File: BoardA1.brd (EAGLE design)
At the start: 44 x 100.5 mm, 17 parts, among them J1 LOAD_CELL1X03-PTH, J2 FEMALE 2x3, J3 LOAD_CELL1X03-PTH, J5 LOAD_CELL1X03-PTH, J6 LOAD_CELL1X03-PTH

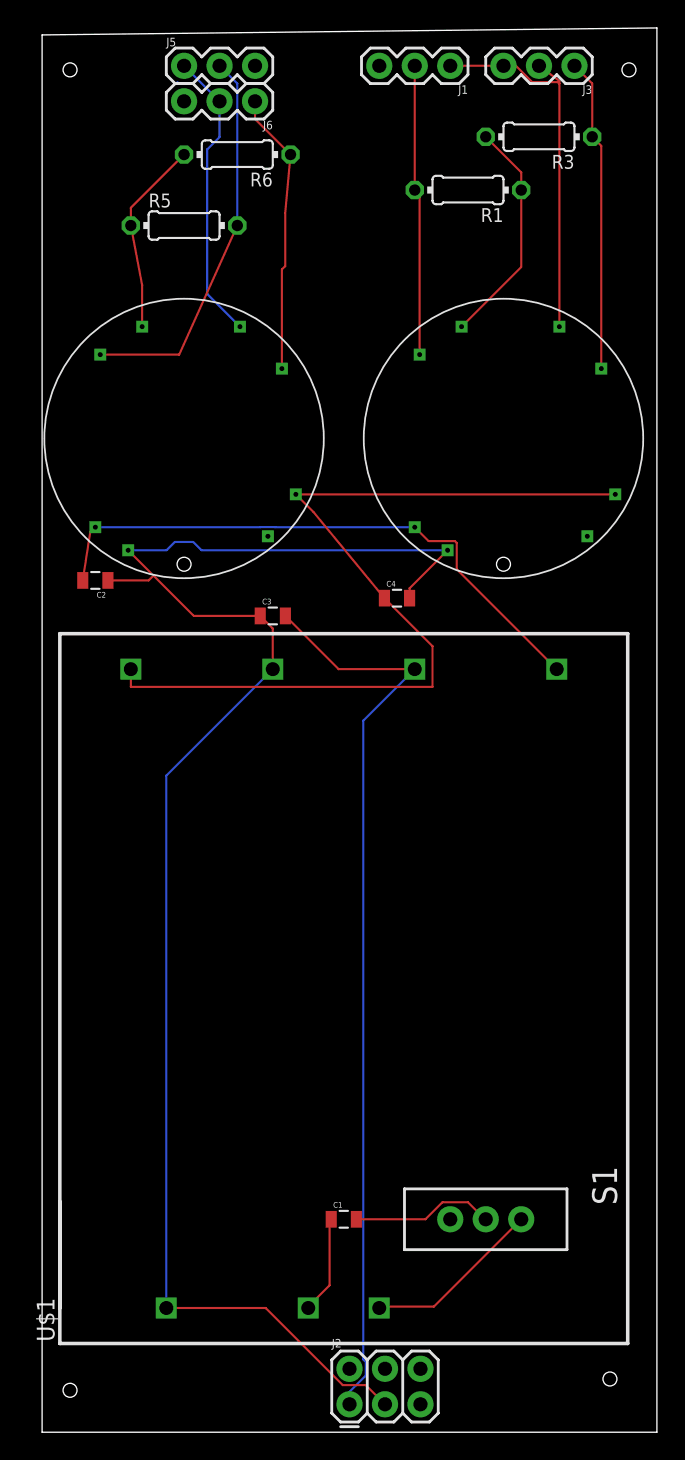
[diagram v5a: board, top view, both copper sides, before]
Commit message: Updated
Fixed Hole placment,connectors, routing issues
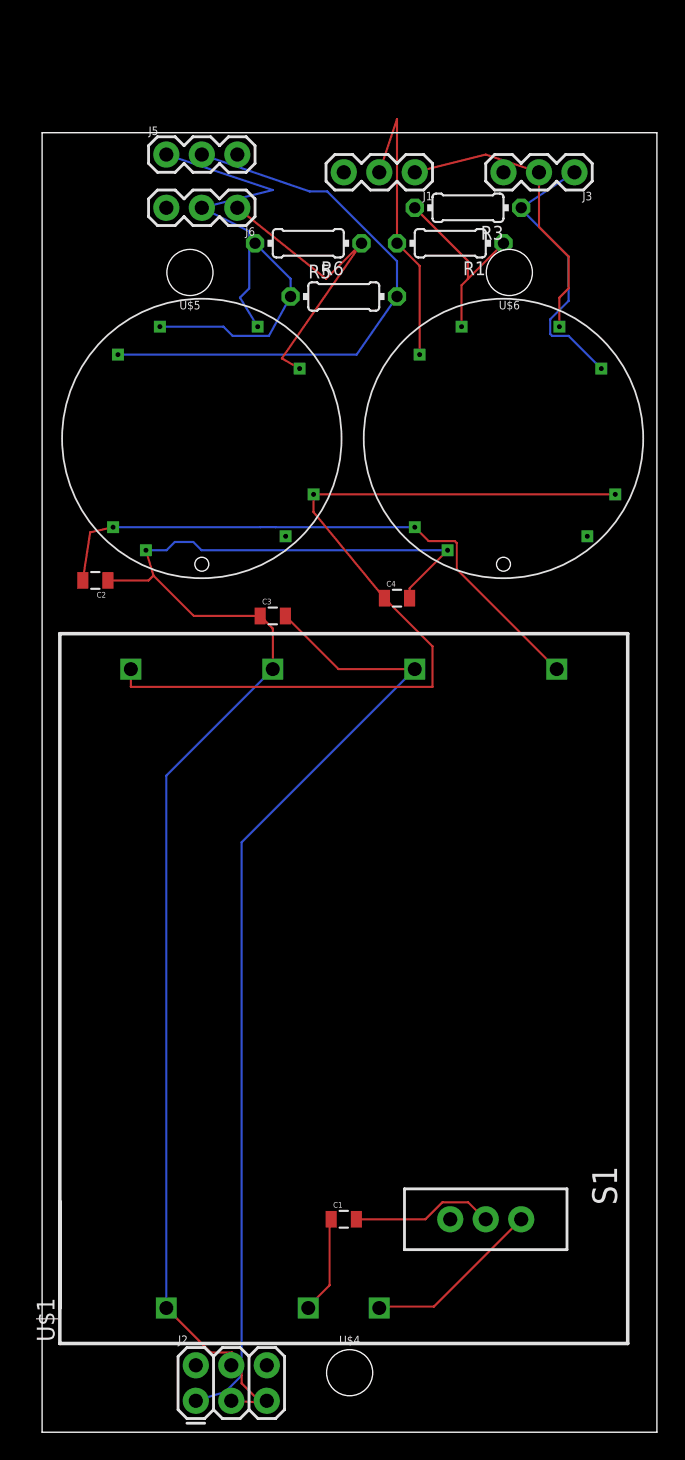
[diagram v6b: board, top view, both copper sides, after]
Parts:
- added U$4, U$5, U$6: (no value), SparkFun-Hardware:STAND-OFF
- moved R5 12.5 mm to (21.6, 81.3)
- moved J2 11.0 mm to (11.0, 2.25)
- moved R6 8.13 mm to (19.1, 85.1)
- moved J1 8.03 mm to (26.7, 90.2)
- moved J6 7.73 mm to (14.0, 87.6)
- moved J3 7.62 mm to (38.1, 90.2)
- moved R3 7.18 mm to (30.5, 87.6)
- moved J5 6.48 mm to (8.89, 91.4)
- moved R1 4.02 mm to (29.2, 85.1)
- moved U$3 1.27 mm to (11.4, 71.1)
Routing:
- net +EX2: track 27.7 -> 41.1 mm
- net GND: track 114.3 -> 106.4 mm
- net -SIG1: track 27.7 -> 21.5 mm
- net 5V: track 65.5 -> 70.4 mm
- net -SIG2: track 21.3 -> 24.5 mm
- net -EX2: track 20.4 -> 23.2 mm
- net +SIG1: track 16.5 -> 13.9 mm
- net -EX1: track 22.6 -> 20.4 mm
- net +SIG2: track 14.2 -> 16.2 mm
- net -15V: track 63.3 -> 61.5 mm
- net +EX1: track 21.0 -> 21.5 mm
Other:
- board size 44 x 100.5 mm -> 44 x 93 mm
